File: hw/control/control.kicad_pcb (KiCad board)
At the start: 2 copper layers, 200 x 100 mm, 143 parts, among them J101 Screw_Terminal_01x02, J102 Screw_Terminal_01x03, J103 Screw_Terminal_01x03, J301 Conn_02x05_Odd_Even, J302 Conn_01x04, J303 Raspberry_Pi_0_2_3, J304 Micro_SD_Card, J305 Conn_01x06, Q1001 BC807, Q1002 BC817, Q401 BC817, Q501 BC817, Q601 BC817, Q701 BC817, Q801 BC807, Q802 BC817, Q901 AOSP21357, Q902 IRF4905, U1001 LM2678T-ADJ, U1101 SN74AHCT125D, U201 LM2596T-ADJ, U801 LM2678T-ADJ

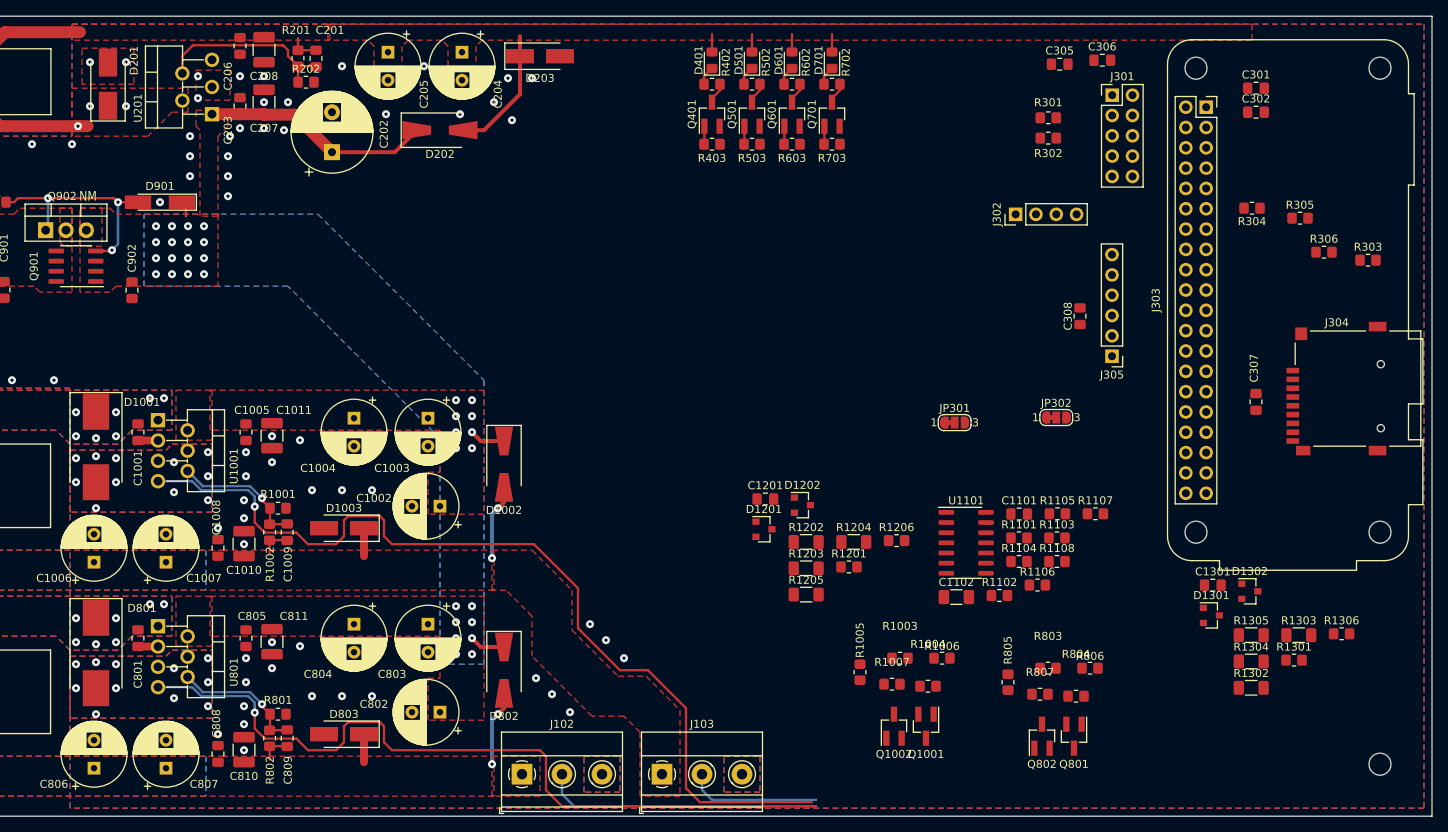
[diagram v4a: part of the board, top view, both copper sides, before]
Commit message: [hw] Add layout of multiple subsystems
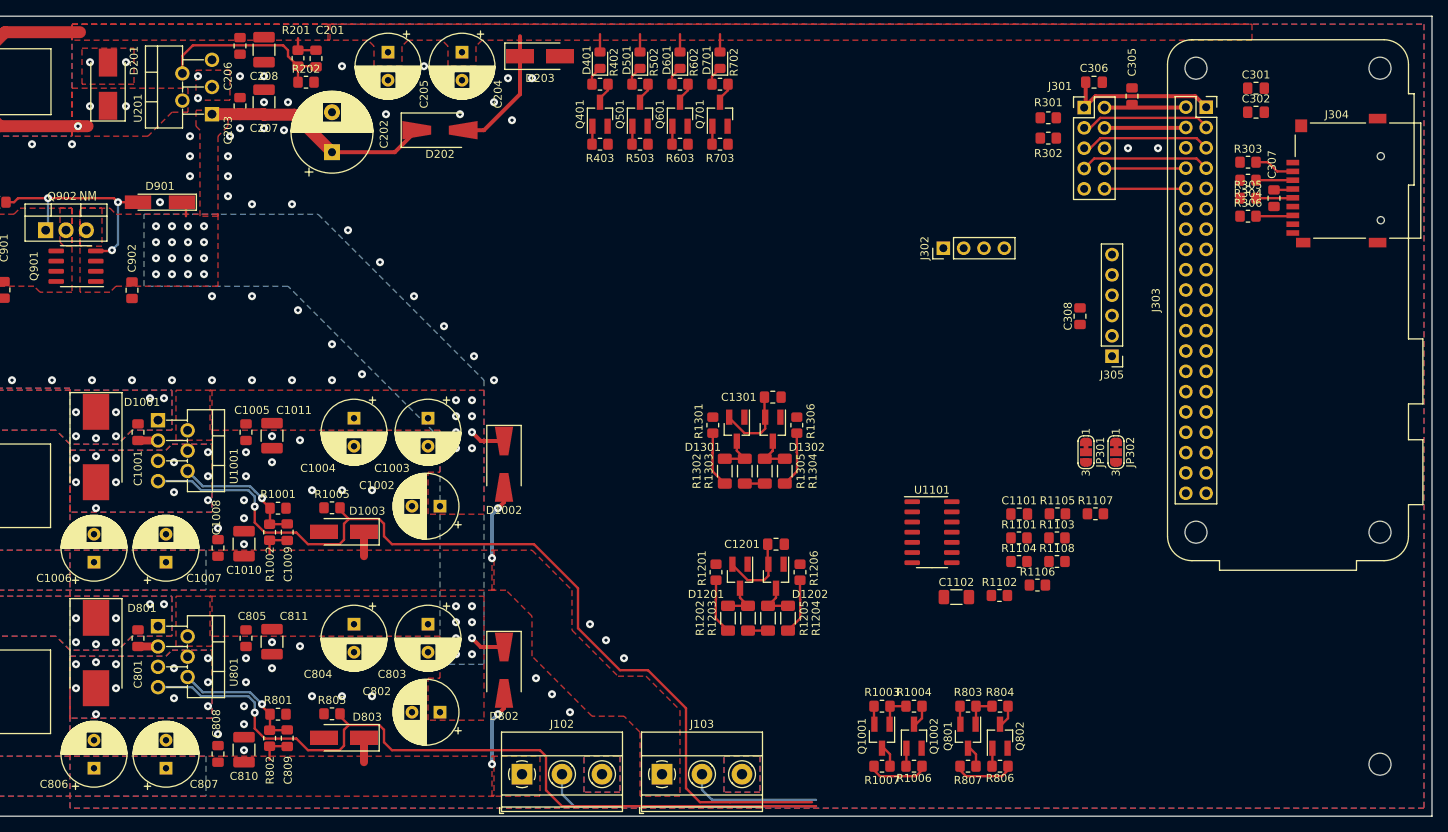
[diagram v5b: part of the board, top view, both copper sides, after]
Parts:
- D1201, D1202, D1301, D1302: footprint Package_TO_SOT_SMD:SOT-23 -> Package_TO_SOT_SMD:SOT-23_Handsoldering
- moved R805 84.6 mm to (102.5, 137.2), turned to 180 degrees
- moved R1301 78.4 mm to (150.1, 101.1), turned to 270 degrees
- moved R1306 72.9 mm to (160.6, 101.1), turned to 90 degrees
- moved R1303 72.2 mm to (154.1, 106.9), turned to 90 degrees
- moved R1302 71.2 mm to (151.6, 106.9), turned to 270 degrees
- moved R1005 69.1 mm to (102.5, 111.5), turned to 180 degrees
- moved R1305 64.2 mm to (156.6, 106.9), turned to 90 degrees
- moved D1301 63.7 mm to (153.1, 101.6), turned to 270 degrees
- moved D1302 63.0 mm to (157.6, 101.6), turned to 270 degrees
- moved R1304 63.0 mm to (159.1, 106.9), turned to 270 degrees
- moved C1301 59.8 mm to (157.6, 97.6)
- moved J304 26.0 mm to (233.6, 70.5)
- moved C307 25.6 mm to (220.2, 72.8)
- moved R303 19.4 mm to (217.0, 68.2)
- moved JP301 16.8 mm to (196.8, 104.5), turned to 270 degrees
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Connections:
- J303 pad 27: (no net) -> Net-(J303-Pad27)
- J303 pad 28: (no net) -> Net-(J303-Pad28)
- J303 pad 29: (no net) -> Net-(J303-Pad29)
- J303 pad 31: (no net) -> Net-(J303-Pad31)
- J303 pad 35: (no net) -> Net-(J303-Pad35)
- J303 pad 36: (no net) -> Net-(J303-Pad36)
- J303 pad 40: (no net) -> Net-(J303-Pad40)
- J304 pad 1: (no net) -> Net-(J304-Pad1)
- J304 pad 8: (no net) -> Net-(J304-Pad8)
- U1001 pad 5: (no net) -> Net-(U1001-Pad5)
- U801 pad 5: (no net) -> Net-(U801-Pad5)
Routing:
- net +5V: track 41.6 -> 85.9 mm
- net +3V3: track 0.00 -> 22.1 mm
- net /CPU/IIC0_SDA: track 0.00 -> 16.3 mm
- net /CPU/GPIO4: track 0.00 -> 16.3 mm
- net /CPU/IIC0_SCL: track 0.00 -> 16.3 mm
- net /CPU/UART_TXD: track 0.00 -> 10.2 mm
- net /CPU/UART_RXD: track 0.00 -> 10.2 mm
- net /LED_PWR_EN1: track 0.00 -> 7.62 mm
- net /LED_PWR_EN0: track 0.00 -> 7.62 mm
- net /LED Driver/LED Driver Output 0/IN_B: track 0.00 -> 6.94 mm
- net /LED Driver/LED Driver Output 0/IN_A: track 0.00 -> 6.94 mm
- net /LED Driver/LED Driver Output 1/IN_B: track 0.00 -> 6.94 mm
- net /LED Driver/LED Driver Output 1/IN_A: track 0.00 -> 6.94 mm
- net Net-(D1202-Pad3): track 0.00 -> 5.11 mm
- net Net-(D1201-Pad3): track 0.00 -> 5.11 mm
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
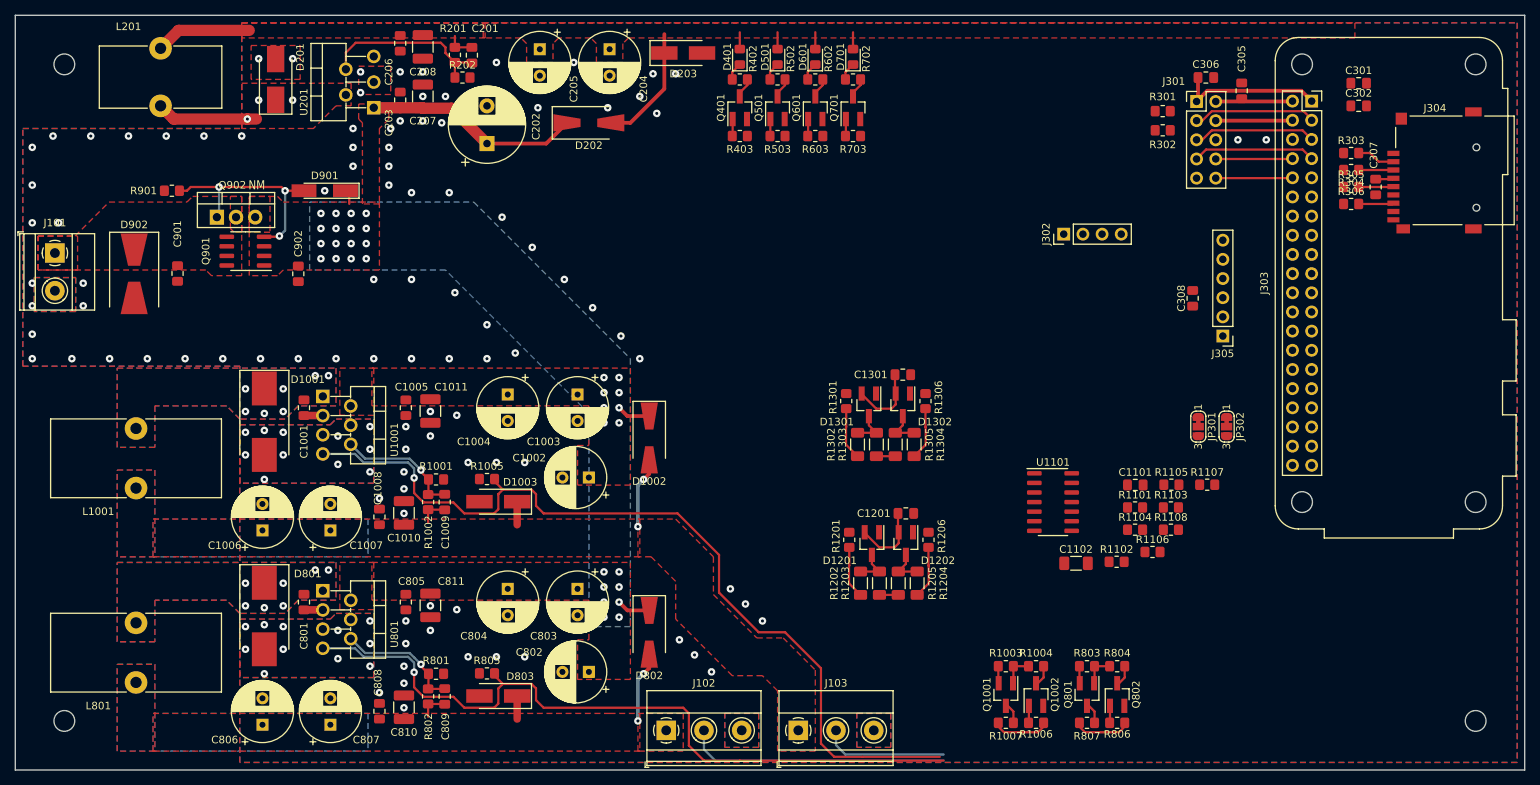
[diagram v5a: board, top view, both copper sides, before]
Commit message: [hw] Improve control layout
Compacted 5V power supply, laid-out SD card holder to the RPi.
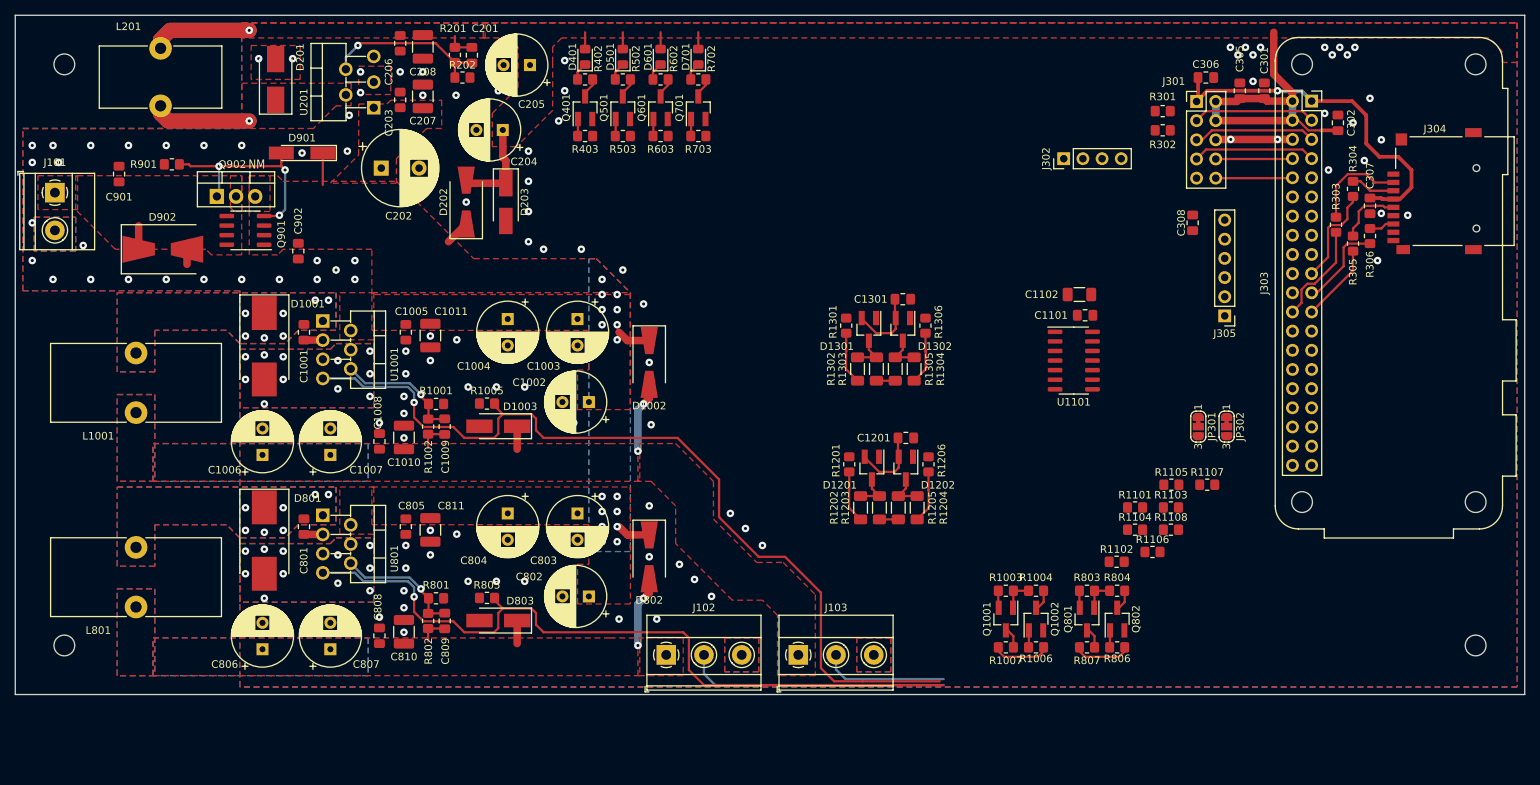
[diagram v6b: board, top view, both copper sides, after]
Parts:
- R402, R502, R602, R702: value 330R -> 1K
- moved C1102 35.6 mm to (181.0, 87.0), turned to 180 degrees
- moved D203 30.7 mm to (105.0, 74.8), turned to 270 degrees
- moved C1101 23.4 mm to (181.8, 89.8), turned to 180 degrees
- moved D401 20.5 mm to (115.5, 55.5)
- moved D501 20.5 mm to (120.5, 55.5)
- moved D601 20.5 mm to (125.5, 55.5)
- moved D701 20.5 mm to (130.5, 55.5)
- moved Q401 20.5 mm to (115.5, 62.2)
- moved Q501 20.5 mm to (120.5, 62.2)
- moved Q601 20.5 mm to (125.5, 62.2)
- moved Q701 20.5 mm to (130.5, 62.2)
- moved R402 20.5 mm to (115.5, 58.5)
- moved R403 20.5 mm to (115.5, 66.0)
- moved R502 20.5 mm to (120.5, 58.5)
- moved R503 20.5 mm to (120.5, 66.0)
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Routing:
- net +5V: track 85.9 -> 118.9 mm, vias 0 -> 1
- net +3V3: track 22.1 -> 47.9 mm, vias 0 -> 1
- net /LED0 Power/VIN: track 39.4 -> 16.5 mm, vias 32 -> 16
- net /CPU/SPI0_CS0: track 0.00 -> 13.5 mm
- net /CPU/SPI0_MOSI: track 0.00 -> 13.3 mm
- net Net-(D201-Pad1): track 13.4 -> 26.3 mm, vias 3 -> 1
- net GND: track 0.00 -> 12.2 mm, vias 122 -> 130
- net /CPU/SPI0_MISO: track 0.00 -> 11.9 mm
- net /CPU/SPI0_CLK: track 0.00 -> 10.3 mm
- net Net-(J304-Pad2): track 5.08 -> 12.8 mm
- net Net-(J304-Pad5): track 4.62 -> 8.55 mm
- net /Input Protection/V_A: track 0.00 -> 3.10 mm
- net Net-(J304-Pad7): track 4.64 -> 3.35 mm
- net Net-(J304-Pad3): track 4.60 -> 5.87 mm
- net Net-(C201-Pad1): track 23.0 -> 22.1 mm, vias 0 -> 1
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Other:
- board size 200 x 100 mm -> 200 x 90 mm

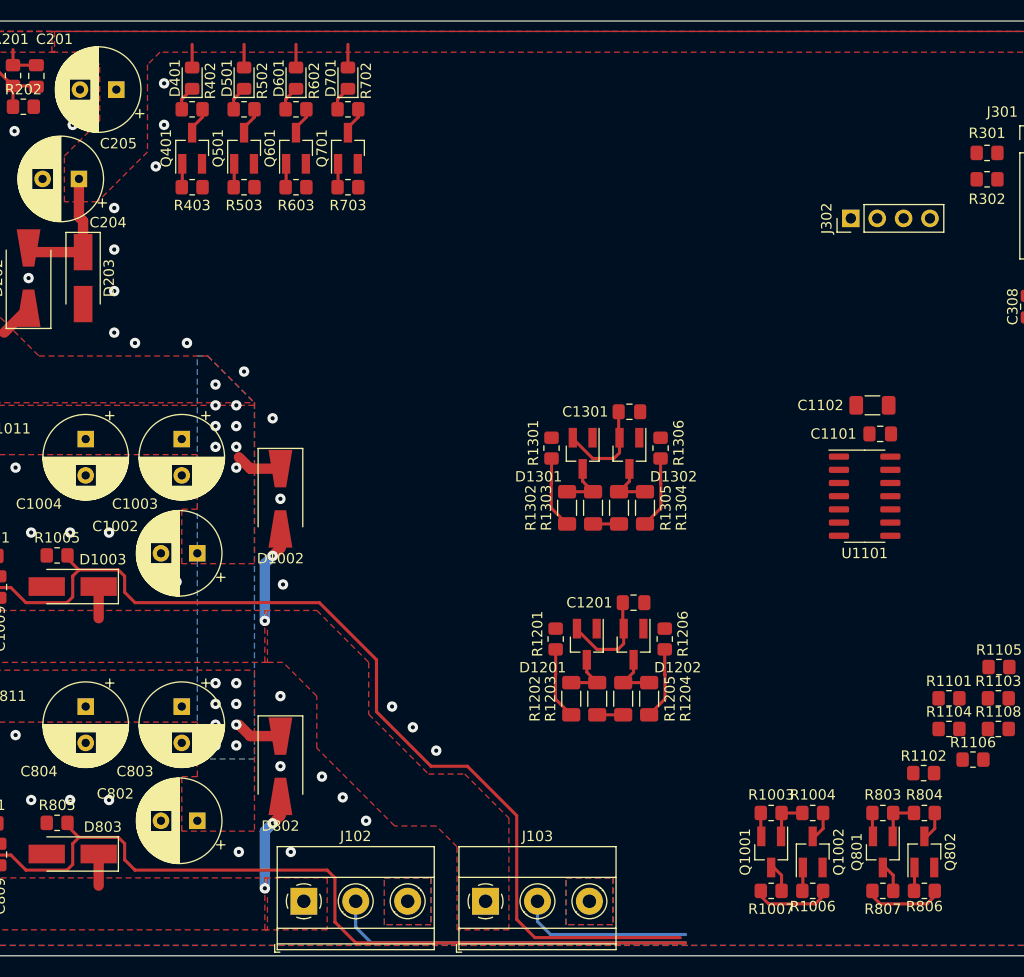
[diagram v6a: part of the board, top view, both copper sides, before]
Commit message: [hw] Add LED power supply enable layout
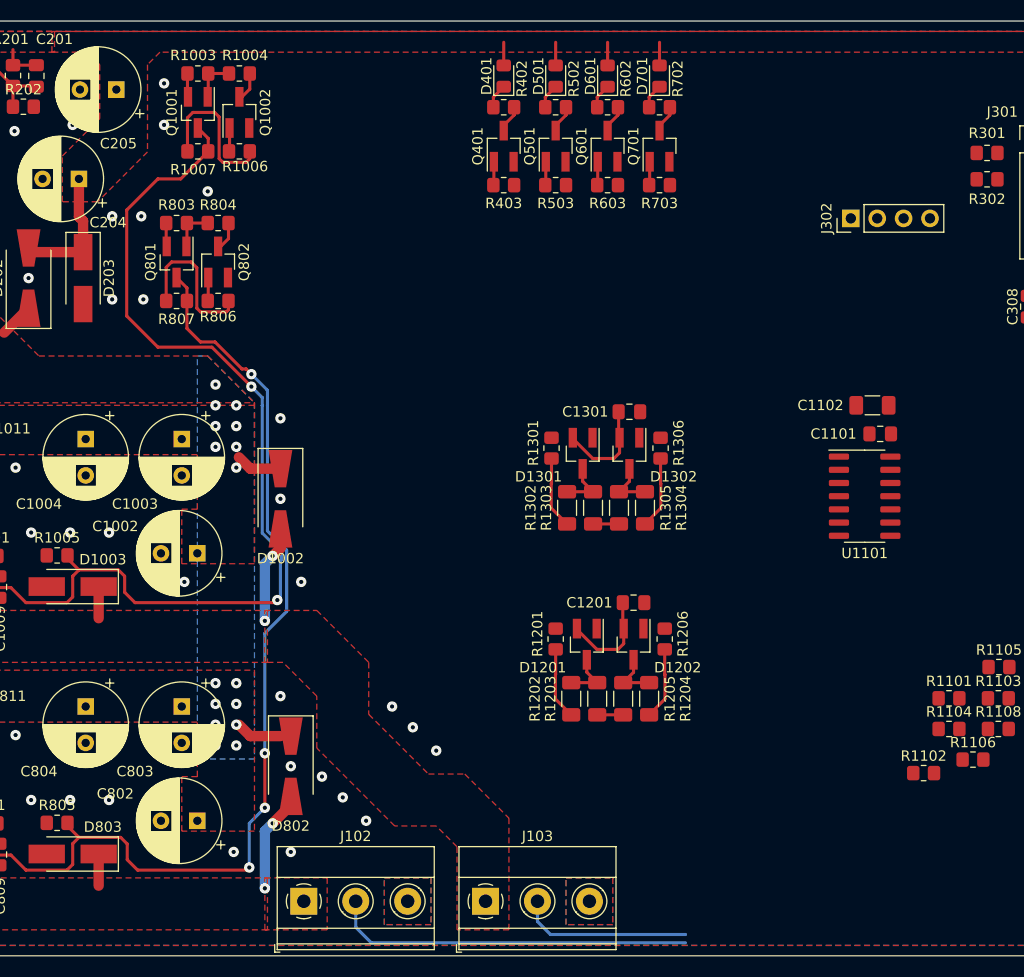
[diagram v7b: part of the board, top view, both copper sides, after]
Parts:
- moved Q1001 90.1 mm to (116.0, 58.8)
- moved Q1002 90.1 mm to (120.0, 58.8)
- moved R1003 90.1 mm to (116.0, 55.0)
- moved R1004 90.1 mm to (120.0, 55.0)
- moved R1006 90.1 mm to (120.0, 62.5)
- moved R1007 90.1 mm to (116.0, 62.5)
- moved Q801 88.6 mm to (114.0, 73.2)
- moved Q802 88.6 mm to (118.0, 73.2)
- moved R803 88.6 mm to (114.0, 69.5)
- moved R804 88.6 mm to (118.0, 69.5)
- moved R806 88.6 mm to (118.0, 77.0)
- moved R807 88.6 mm to (114.0, 77.0)
- moved D401 30.0 mm to (145.5, 55.3)
- moved D501 30.0 mm to (150.5, 55.3)
- moved D601 30.0 mm to (155.5, 55.3)
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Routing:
- net /LED0 Power/ENABLE: track 102.2 -> 115.8 mm, vias 1 -> 5
- net /LED_PWR_EN0: track 7.62 -> 14.7 mm
- net /LED_PWR_EN1: track 7.62 -> 14.6 mm
- net /LED1 Power/ENABLE: track 118.4 -> 114.5 mm, vias 1 -> 3
- net GND: vias 130 -> 127
